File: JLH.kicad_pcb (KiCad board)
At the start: 2 copper layers, 5 parts, among them Q1 КТ361Г, Q2 КТ801А, Q3 2Т803А, Q4 2Т803А

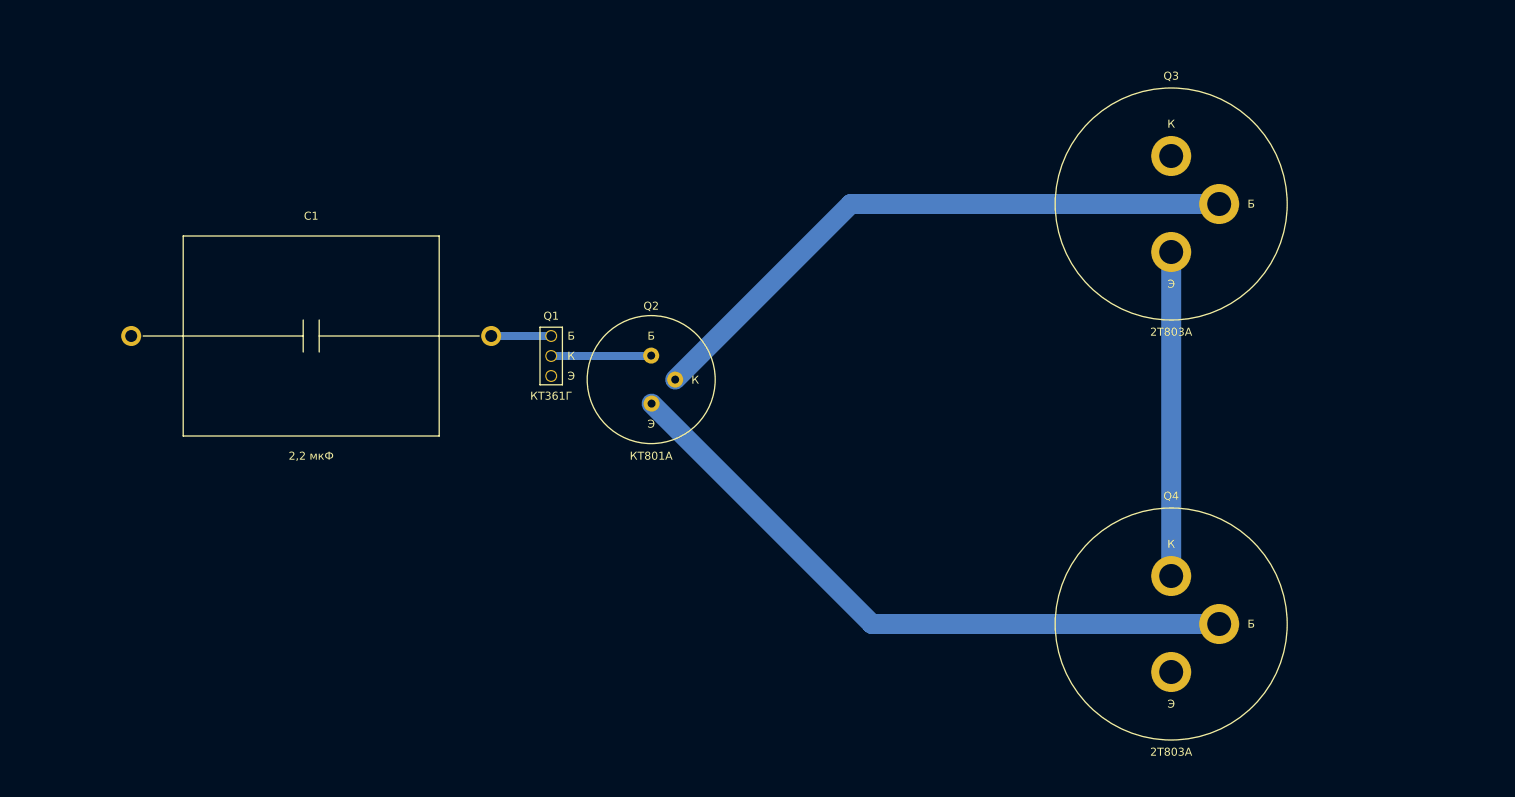
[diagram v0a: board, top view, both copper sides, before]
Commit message: Updated PCB (one channel)
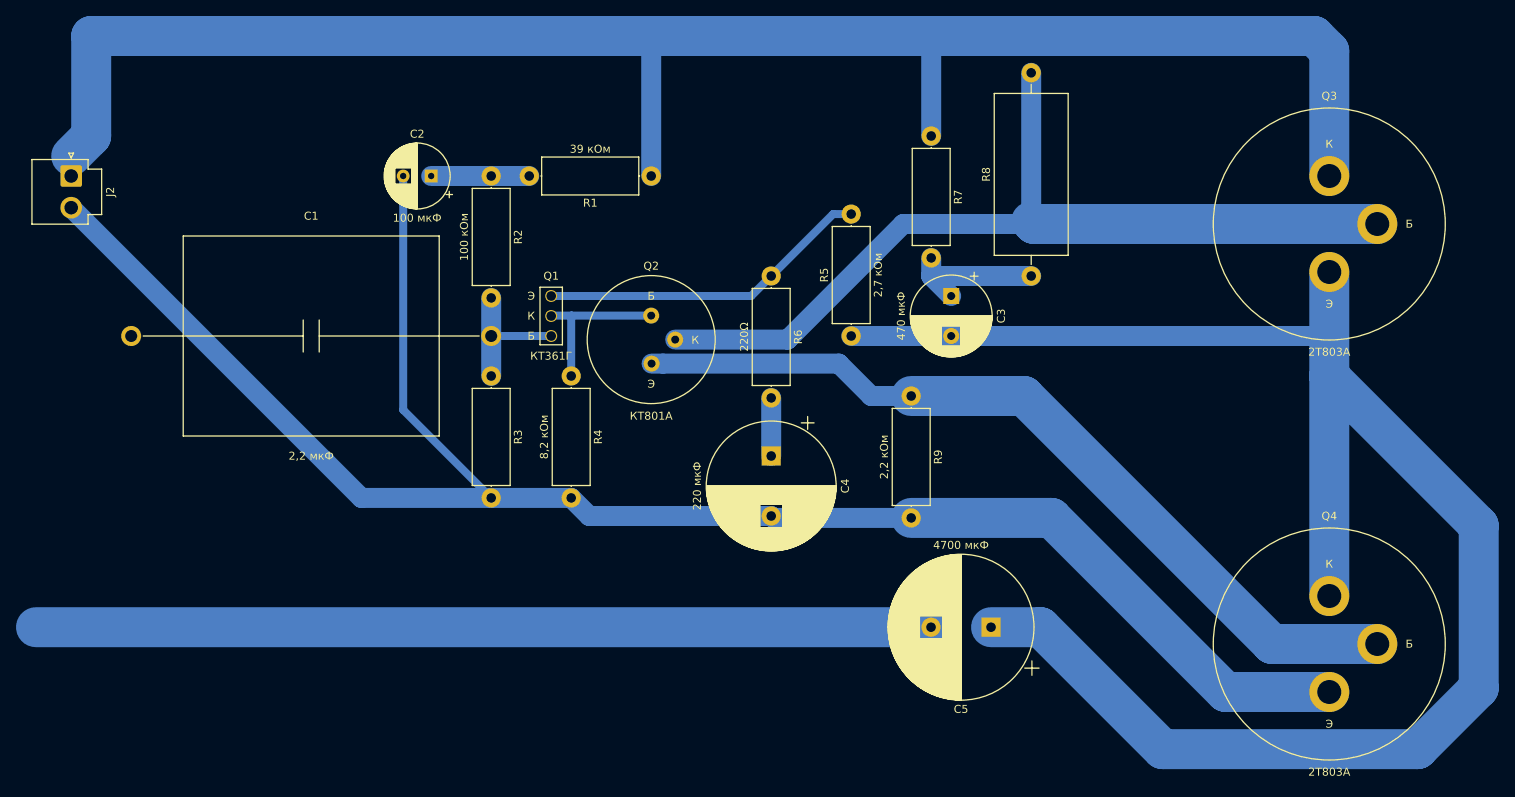
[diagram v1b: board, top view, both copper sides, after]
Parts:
- added C2: 100 мкФ, Capacitor_THT:CP_Radial_D8.0mm_P3.50mm, F.Cu at (87.5, 32.5)
- added C3: 470 мкФ, Capacitor_THT:CP_Radial_D10.0mm_P5.00mm, F.Cu at (152.5, 47.5)
- added C4: 220 мкФ, Capacitor_THT:CP_Radial_D16.0mm_P7.50mm, F.Cu at (130.0, 67.5)
- added C5: 4700 мкФ, Capacitor_THT:CP_Radial_D18.0mm_P7.50mm, F.Cu at (157.5, 88.9)
- added J2: B2P-VH, Connector_JST:JST_VH_B2P-VH_1x02_P3.96mm_Vertical, F.Cu at (42.5, 32.5)
- added R1: 39 кОм, Resistor_THT:R_Axial_DIN0414_L11.9mm_D4.5mm_P15.24mm_Horizontal, F.Cu at (115.0, 32.5)
- added R2: 100 кОм, Resistor_THT:R_Axial_DIN0414_L11.9mm_D4.5mm_P15.24mm_Horizontal, F.Cu at (95.0, 32.5)
- added R3: 100 кОм*, Resistor_THT:R_Axial_DIN0414_L11.9mm_D4.5mm_P15.24mm_Horizontal, F.Cu at (95.0, 57.5)
- added R4: 8,2 кОм, Resistor_THT:R_Axial_DIN0414_L11.9mm_D4.5mm_P15.24mm_Horizontal, F.Cu at (105.0, 57.5)
- added R5: 2,7 кОм, Resistor_THT:R_Axial_DIN0414_L11.9mm_D4.5mm_P15.24mm_Horizontal, F.Cu at (140.0, 52.5)
- added R6: 220Ω, Resistor_THT:R_Axial_DIN0414_L11.9mm_D4.5mm_P15.24mm_Horizontal, F.Cu at (130.0, 45.0)
- added R7: 47Ω*, Resistor_THT:R_Axial_DIN0414_L11.9mm_D4.5mm_P15.24mm_Horizontal, F.Cu at (150.0, 27.5)
- added R8: 180Ω*, Resistor_THT:R_Axial_DIN0922_L20.0mm_D9.0mm_P25.40mm_Horizontal, F.Cu at (162.5, 45.0)
- added R9: 2,2 кОм, Resistor_THT:R_Axial_DIN0414_L11.9mm_D4.5mm_P15.24mm_Horizontal, F.Cu at (147.5, 60.0)
- moved Q3 19.9 mm to (199.8, 32.5)
- moved Q4 19.9 mm to (199.8, 85.0)
- moved Q1 10.0 mm to (102.5, 47.5), turned to 270 degrees
- moved Q2 5.00 mm to (115.0, 50.0)
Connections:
- Q1 pad 1: (no net) -> Net-(Q1-Pad1)
- Q3 pad 1: (no net) -> Net-(J2-Pad1)
- Q4 pad 3: (no net) -> GND
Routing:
- net GND: track 0.00 -> 227.1 mm
- net Net-(J2-Pad1): track 0.00 -> 219.7 mm
- net Net-(C3-Pad2): track 40.5 -> 217.4 mm
- net (no net): track 0.00 -> 111.9 mm
- net Net-(Q2-Pad2): track 77.1 -> 171.4 mm
- net Net-(Q1-Pad1): track 0.00 -> 41.7 mm
- net Net-(Q2-Pad3): track 82.4 -> 105.2 mm
- net Net-(C3-Pad1): track 0.00 -> 18.3 mm
- net Net-(C2-Pad1): track 0.00 -> 12.3 mm
- net Net-(C1-Pad2): track 7.50 -> 17.3 mm
- net Net-(Q1-Pad2): track 12.5 -> 20.1 mm
- net Net-(C4-Pad1): track 0.00 -> 7.26 mm

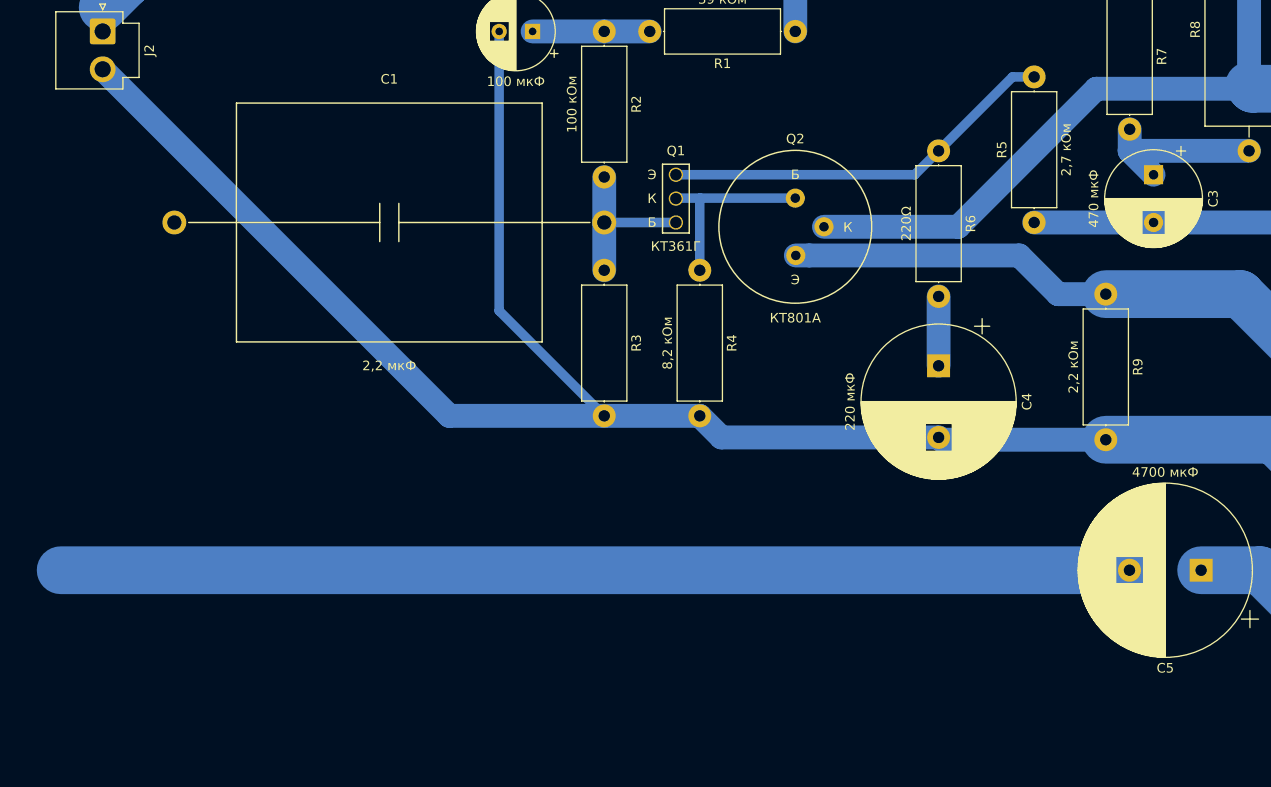
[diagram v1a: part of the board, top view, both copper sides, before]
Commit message: Added I/O terminals
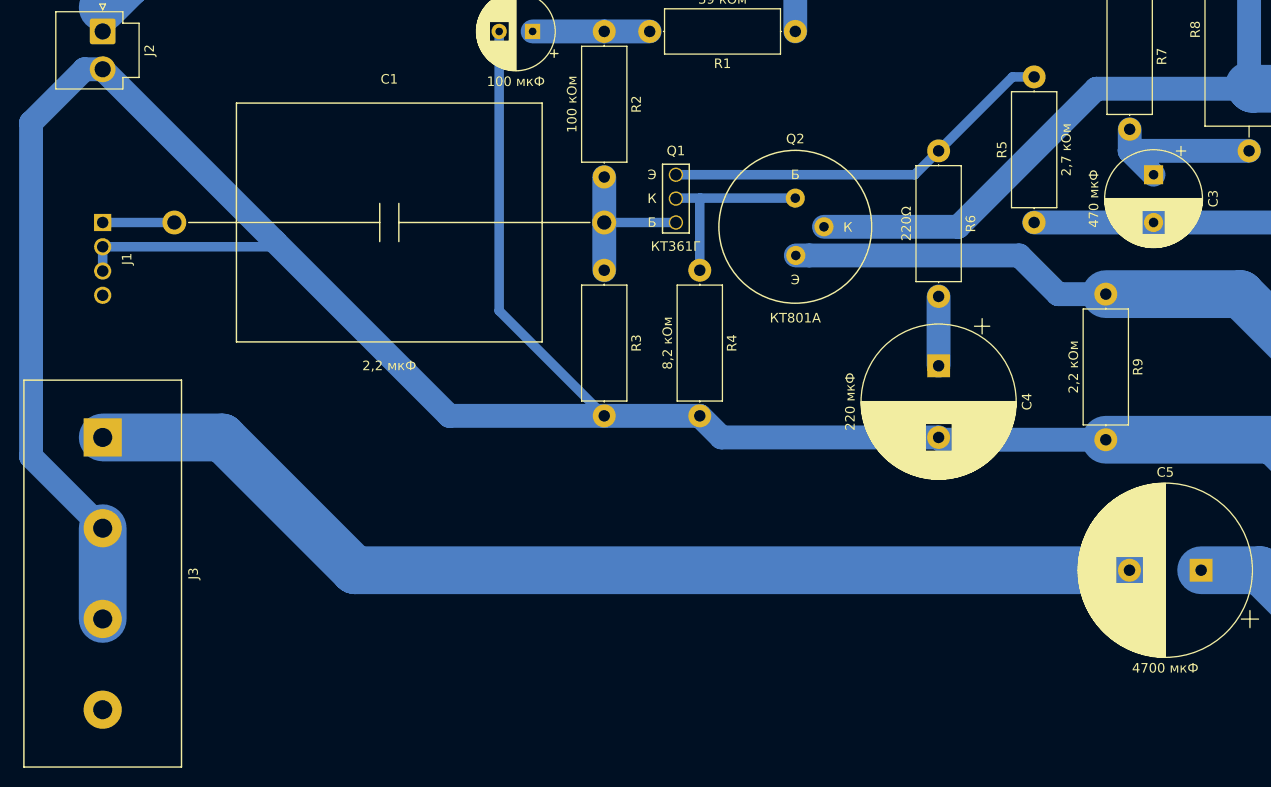
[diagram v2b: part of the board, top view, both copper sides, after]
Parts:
- added J1: 5-103639-3, JLH:5-103639-3, F.Cu at (42.5, 52.5)
- added J3: T34-BM11-04, JLH:T34-BM11-04, F.Cu at (42.5, 75.0)
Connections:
- C1 pad 1: (no net) -> Net-(C1-Pad1)
- C5 pad 2: (no net) -> Net-(C5-Pad2)
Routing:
- net Net-(C5-Pad2): track 0.00 -> 113.2 mm
- net (no net): track 111.9 -> 0.00 mm
- net GND: track 227.1 -> 312.8 mm
- net Net-(C1-Pad1): track 0.00 -> 7.50 mm

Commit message: Updated PCB
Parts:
- removed C1: 2,2 мкФ, JLH:KZK_White_Line_L32.0mm_D25.0mm_P45.00mm_Horizontal
- added C10: 100 мкФ, Capacitor_THT:CP_Radial_D8.0mm_P3.50mm, F.Cu at (60.0, 202.0)
- added C11: 470 мкФ, Capacitor_THT:CP_Radial_D10.0mm_P5.00mm, F.Cu at (117.5, 179.5)
- added C12: 220 мкФ, Capacitor_THT:CP_Radial_D16.0mm_P7.50mm, F.Cu at (91.5, 174.5)
- added C14: 4700 мкФ, Capacitor_THT:CP_Radial_D18.0mm_P7.50mm, F.Cu at (130.0, 154.5)
- added C7: 4700 мкФ, Capacitor_THT:CP_Radial_D18.0mm_P7.50mm, F.Cu at (130.0, 97.5)
- added C9: 2,2 мкФ, JLH:KZK_White_Line_L32.0mm_D25.0mm_P45.00mm_Horizontal, F.Cu at (45.0, 152.0)
- added D1: LED, LED_THT:LED_D5.0mm, F.Cu at (63.0, 112.5)
- added Q5: КТ361Г, JLH:kt-13, F.Cu at (72.5, 187.0)
- added Q6: КТ801А, JLH:kt801, F.Cu at (83.9, 191.5)
- added Q7: 2Т803А, JLH:2t803a, F.Cu at (165.0, 207.0)
- added Q8: 2Т803А, JLH:2t803a, F.Cu at (165.0, 157.0)
- added R10: 2,2 кОм, Resistor_THT:R_Axial_DIN0414_L11.9mm_D4.5mm_P15.24mm_Horizontal, F.Cu at (107.5, 75.0)
- added R11: 39 кОм, Resistor_THT:R_Axial_DIN0414_L11.9mm_D4.5mm_P15.24mm_Horizontal, F.Cu at (82.5, 202.0)
- added R12: 100 кОм, Resistor_THT:R_Axial_DIN0414_L11.9mm_D4.5mm_P15.24mm_Horizontal, F.Cu at (65.0, 197.0)
- added R13: 100 кОм, Resistor_THT:R_Axial_DIN0414_L11.9mm_D4.5mm_P15.24mm_Horizontal, F.Cu at (65.0, 177.0)
- added R14: 8,2 кОм, Resistor_THT:R_Axial_DIN0414_L11.9mm_D4.5mm_P15.24mm_Horizontal, F.Cu at (75.0, 177.0)
- added R15: 2,7 кОм, Resistor_THT:R_Axial_DIN0414_L11.9mm_D4.5mm_P15.24mm_Horizontal, F.Cu at (107.5, 197.0)
- added R16: 220Ω, Resistor_THT:R_Axial_DIN0414_L11.9mm_D4.5mm_P15.24mm_Horizontal, F.Cu at (97.5, 197.0)
- added R17: 47Ω, Resistor_THT:R_Axial_DIN0414_L11.9mm_D4.5mm_P15.24mm_Horizontal, F.Cu at (117.5, 202.0)
- added R18: 180Ω, Resistor_THT:R_Axial_DIN0922_L20.0mm_D9.0mm_P25.40mm_Horizontal, F.Cu at (130.0, 197.0)
- added R19: 2,2 кОм, Resistor_THT:R_Axial_DIN0414_L11.9mm_D4.5mm_P15.24mm_Horizontal, F.Cu at (107.5, 177.0)
- C2: value 100 мкФ -> 2,2 мкФ; footprint Capacitor_THT:CP_Radial_D8.0mm_P3.50mm -> JLH:KZK_White_Line_L32.0mm_D25.0mm_P45.00mm_Horizontal
- C3: value 470 мкФ -> 100 мкФ; footprint Capacitor_THT:CP_Radial_D10.0mm_P5.00mm -> Capacitor_THT:CP_Radial_D8.0mm_P3.50mm
- C4: value 220 мкФ -> 470 мкФ; footprint Capacitor_THT:CP_Radial_D16.0mm_P7.50mm -> Capacitor_THT:CP_Radial_D10.0mm_P5.00mm
- C5: value 4700 мкФ -> 220 мкФ; footprint Capacitor_THT:CP_Radial_D18.0mm_P7.50mm -> Capacitor_THT:CP_Radial_D16.0mm_P7.50mm
- J1: value 5-103639-3 -> Вход
- J2: value B2P-VH -> Выход; footprint Connector_JST:JST_VH_B2P-VH_1x02_P3.96mm_Vertical -> JLH:T34-BM11-04
- J3: value T34-BM11-04 -> B2P-VH; footprint JLH:T34-BM11-04 -> Connector_JST:JST_VH_B2P-VH_1x02_P3.96mm_Vertical
- R1: value 39 кОм -> 2,2 кОм
- R2: value 100 кОм -> 39 кОм
- R3: value 100 кОм* -> 100 кОм
- R4: value 8,2 кОм -> 100 кОм
- R5: value 2,7 кОм -> 8,2 кОм
- R6: value 220Ω -> 2,7 кОм
- R7: value 47Ω* -> 220Ω
- R8: value 180Ω* -> 47Ω; footprint Resistor_THT:R_Axial_DIN0922_L20.0mm_D9.0mm_P25.40mm_Horizontal -> Resistor_THT:R_Axial_DIN0414_L11.9mm_D4.5mm_P15.24mm_Horizontal
- R9: value 2,2 кОм -> 180Ω; footprint Resistor_THT:R_Axial_DIN0414_L11.9mm_D4.5mm_P15.24mm_Horizontal -> Resistor_THT:R_Axial_DIN0922_L20.0mm_D9.0mm_P25.40mm_Horizontal
- moved C3 92.5 mm to (60.0, 50.0), turned to 180 degrees
- moved R1 85.3 mm to (85.5, 112.5)
- moved J2 80.6 mm to (32.5, 112.5)
- moved C2 79.8 mm to (45.0, 100.0), turned to 90 degrees
- moved J1 71.1 mm to (55.0, 122.5)
- moved R5 68.8 mm to (75.0, 75.0), turned to 270 degrees
- moved C5 67.0 mm to (91.5, 77.5), turned to 270 degrees
- moved J3 66.7 mm to (85.5, 126.0), turned to 180 degrees
- moved R7 59.3 mm to (97.5, 55.0)
- moved R8 45.3 mm to (117.5, 50.0), turned to 270 degrees
- moved R4 43.7 mm to (65.0, 75.0)
- moved Q3 36.9 mm to (165.0, 45.0)
- moved Q4 36.2 mm to (165.0, 95.0)
- moved Q1 34.7 mm to (72.5, 65.0)
- moved Q2 32.9 mm to (83.9, 60.5)
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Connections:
- C2 pad 1: Net-(C2-Pad1) -> /Левый канал/IN+
- C2 pad 2: GND -> Net-(C2-Pad2)
- C3 pad 2: Net-(C3-Pad2) -> GND
- C4 pad 2: GND -> Net-(C4-Pad2)
- C5 pad 1: Net-(C3-Pad2) -> Net-(C5-Pad1)
- C5 pad 2: Net-(C5-Pad2) -> GND
- J1 pad 1: Net-(C1-Pad1) -> /Левый канал/IN+
- J1 pad 4: (no net) -> /Правый канал/IN+
- J2 pad 1: Net-(J2-Pad1) -> /Левый канал/OUT+
- J3 pad 1: Net-(C5-Pad2) -> /Левый канал/VCC
- Q1 pad 3: Net-(C1-Pad2) -> Net-(C2-Pad2)
- Q3 pad 1: Net-(J2-Pad1) -> /Левый канал/VCC
- Q3 pad 3: Net-(C3-Pad2) -> Net-(C4-Pad2)
- Q4 pad 1: Net-(C3-Pad2) -> Net-(C4-Pad2)
- R1 pad 1: Net-(J2-Pad1) -> /Левый канал/VCC
- R1 pad 2: Net-(C2-Pad1) -> Net-(D1-Pad2)
- R2 pad 1: Net-(C2-Pad1) -> /Левый канал/VCC
- R2 pad 2: Net-(C1-Pad2) -> Net-(C3-Pad1)
- R3 pad 1: Net-(C1-Pad2) -> Net-(C3-Pad1)
- R3 pad 2: GND -> Net-(C2-Pad2)
- R4 pad 1: Net-(Q1-Pad2) -> Net-(C2-Pad2)
- R5 pad 1: Net-(C3-Pad2) -> Net-(Q1-Pad2)
- R5 pad 2: Net-(Q1-Pad1) -> GND
- R6 pad 2: Net-(C4-Pad1) -> Net-(C4-Pad2)
- R7 pad 1: Net-(J2-Pad1) -> Net-(Q1-Pad1)
- R7 pad 2: Net-(C3-Pad1) -> Net-(C5-Pad1)
- R8 pad 1: Net-(C3-Pad1) -> /Левый канал/VCC
- R8 pad 2: Net-(Q2-Pad2) -> Net-(C4-Pad1)
- R9 pad 1: Net-(Q2-Pad3) -> Net-(Q2-Pad2)
- R9 pad 2: GND -> Net-(C4-Pad1)
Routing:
- net /Левый канал/VCC: track 0.00 -> 564.9 mm
- net GND: track 312.8 -> 621.1 mm
- net Net-(J2-Pad1): track 219.7 -> 0.00 mm
- net Net-(C3-Pad2): track 217.4 -> 0.00 mm
- net Net-(C4-Pad2): track 0.00 -> 199.6 mm
- net Net-(C11-Pad2): track 0.00 -> 199.6 mm
- net Net-(C5-Pad2): track 113.2 -> 0.00 mm
- net /Левый канал/OUT+: track 0.00 -> 111.2 mm
- net /Правый канал/OUT+: track 0.00 -> 109.7 mm
- net Net-(Q6-Pad3): track 0.00 -> 90.4 mm
- net Net-(Q6-Pad2): track 0.00 -> 83.1 mm
- net Net-(Q2-Pad2): track 171.4 -> 89.3 mm
- net Net-(C2-Pad2): track 0.00 -> 42.5 mm
- net Net-(C9-Pad2): track 0.00 -> 42.5 mm
- net Net-(Q5-Pad1): track 0.00 -> 39.0 mm
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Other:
- board outline added: 170 x 202 mm
- board text added: "+"
